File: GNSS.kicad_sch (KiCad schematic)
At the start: 13 parts, among them J8 USB_C_USB2.0_16P, SW5 SW_Push, U6 NEO-M9N

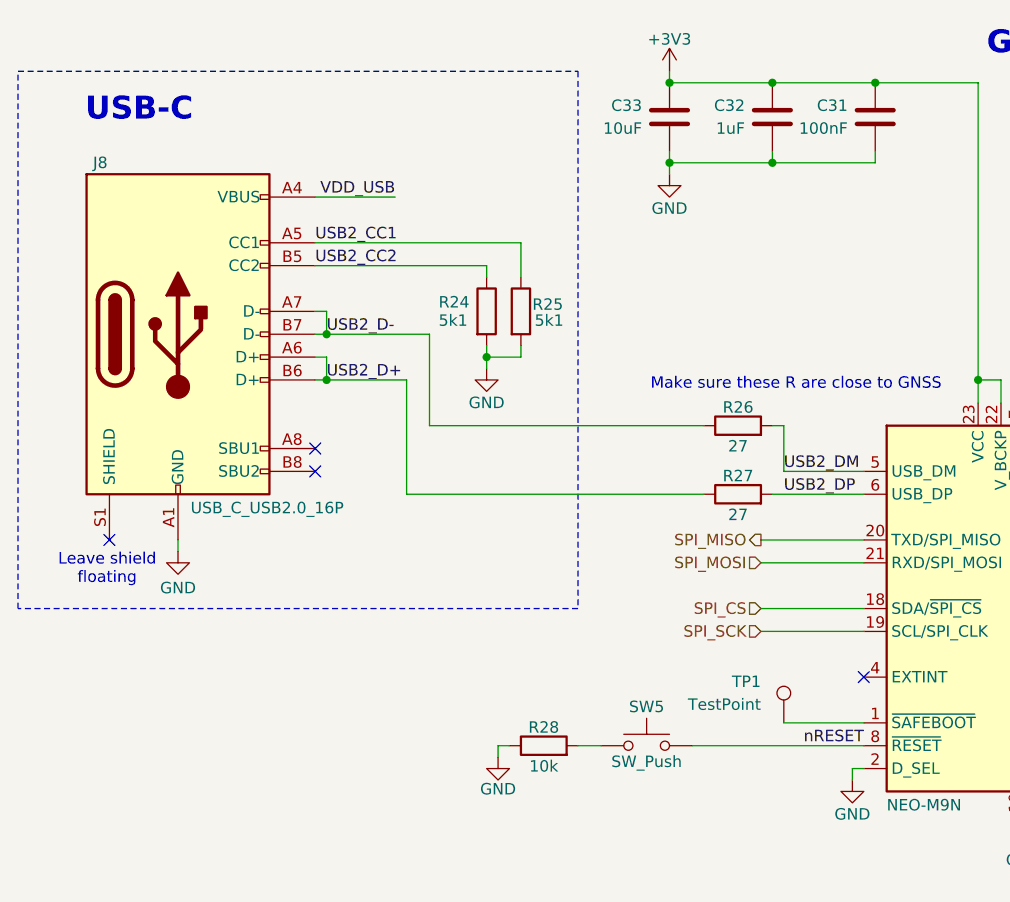
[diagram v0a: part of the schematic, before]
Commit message: Added footprints & routing 30%
- Added Dupont debug headers for UARTs.
- Added footprints: 18650 battery, E32-400M30S.
- Remove Battery Charger due to reliability issue.
- Routing 5V SMPS, 3V3 Regulator, Battery Holder.
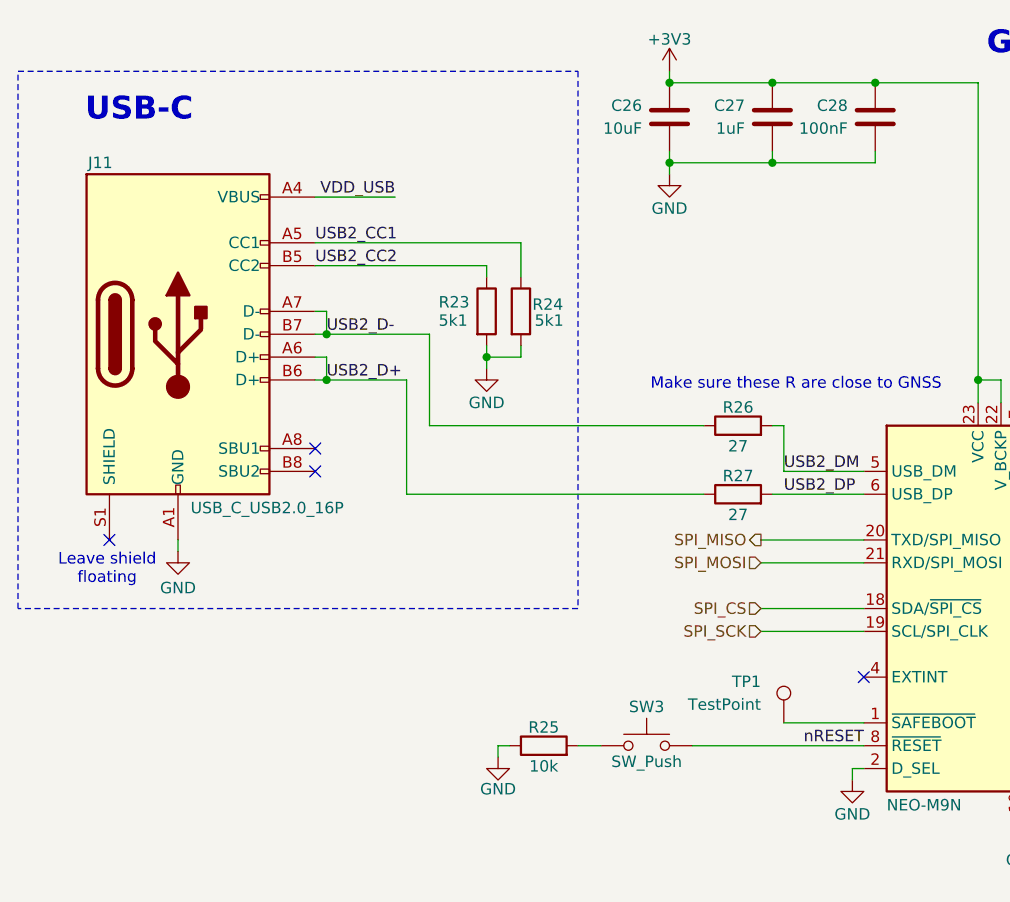
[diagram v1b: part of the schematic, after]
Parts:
- TP1: footprint (none) -> TestPoint:TestPoint_Pad_D2.5mm
- renumbered C33 to C26, C32 to C27, C31 to C28, J8 to J11, R24 to R23, R25 to R24, R28 to R25, SW5 to SW3
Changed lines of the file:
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@@
 		(on_board yes)
 		(dnp no)
-		(property "Reference" "#PWR079"
+		(property "Reference" "#PWR060"
 			(at 118.11 142.24 0)
 			(effects
@@
 			(project "BLV_PCB"
 				(path "/e98ed281-6a46-49b2-ab41-e3d95fdf6973/e5b94b9f-016b-443f-970f-ae0598cc0fac"
-					(reference "#PWR079")
+					(reference "#PWR060")
 					(unit 1)
 				)
@@
 		(on_board yes)
 		(dnp no)
-		(property "Reference" "R28"
+		(property "Reference" "R25"
 			(at 83.82 130.048 90)
 			(effects
@@
 			(project ""
 				(path "/e98ed281-6a46-49b2-ab41-e3d95fdf6973/e5b94b9f-016b-443f-970f-ae0598cc0fac"
-					(reference "R28")
+					(reference "R25")
 					(unit 1)
 				)
@@
 		(on_board yes)
 		(dnp no)
-		(property "Reference" "SW5"
+		(property "Reference" "SW3"
 			(at 95.25 127.762 0)
 			(effects
@@
 			(project "BLV_PCB"
 				(path "/e98ed281-6a46-49b2-ab41-e3d95fdf6973/e5b94b9f-016b-443f-970f-ae0598cc0fac"
-					(reference "SW5")
+					(reference "SW3")
 					(unit 1)
 				)
@@
 		(on_board yes)
 		(dnp no)
-		(property "Reference" "#PWR014"
+		(property "Reference" "#PWR056"
 			(at 77.47 96.52 0)
 			(effects
@@
 			(project "BLV_PCB"
 				(path "/e98ed281-6a46-49b2-ab41-e3d95fdf6973/e5b94b9f-016b-443f-970f-ae0598cc0fac"
-					(reference "#PWR014")
+					(reference "#PWR056")
 					(unit 1)
 				)
@@
 		(on_board yes)
 		(dnp no)
-		(property "Reference" "R24"
+		(property "Reference" "R23"
 			(at 72.136 82.804 0)
 			(effects
@@
 			(project "BLV_PCB"
 				(path "/e98ed281-6a46-49b2-ab41-e3d95fdf6973/e5b94b9f-016b-443f-970f-ae0598cc0fac"
-					(reference "R24")
+					(reference "R23")
 					(unit 1)
 				)
@@
 		(on_board yes)
 		(dnp no)
-		(property "Reference" "#PWR038"
+		(property "Reference" "#PWR055"
 			(at 43.18 116.84 0)
 			(effects
@@
 			(project "BLV_PCB"
 				(path "/e98ed281-6a46-49b2-ab41-e3d95fdf6973/e5b94b9f-016b-443f-970f-ae0598cc0fac"
-					(reference "#PWR038")
+					(reference "#PWR055")
 					(unit 1)
 				)
@@
 		(on_board yes)
 		(dnp no)
-		(property "Reference" "#PWR078"
+		(property "Reference" "#PWR059"
 			(at 97.79 74.93 0)
 			(effects
@@
 			(project "BLV_PCB"
 				(path "/e98ed281-6a46-49b2-ab41-e3d95fdf6973/e5b94b9f-016b-443f-970f-ae0598cc0fac"
-					(reference "#PWR078")
+					(reference "#PWR059")
 					(unit 1)
 				)
@@
 		(on_board yes)
 		(dnp no)
-		(property "Reference" "C32"
+		(property "Reference" "C27"
 			(at 106.172 60.96 0)
 			(effects
@@
 			(project "BLV_PCB"
 				(path "/e98ed281-6a46-49b2-ab41-e3d95fdf6973/e5b94b9f-016b-443f-970f-ae0598cc0fac"
-					(reference "C32")
+					(reference "C27")
 					(unit 1)
 				)
@@
 		(on_board yes)
 		(dnp no)
-		(property "Reference" "C31"
+		(property "Reference" "C28"
 			(at 117.602 60.96 0)
 			(effects
@@
 			(project "BLV_PCB"
 				(path "/e98ed281-6a46-49b2-ab41-e3d95fdf6973/e5b94b9f-016b-443f-970f-ae0598cc0fac"
-					(reference "C31")
+					(reference "C28")
 					(unit 1)
 				)
@@
 		(on_board yes)
 		(dnp no)
-		(property "Reference" "R25"
+		(property "Reference" "R24"
 			(at 82.55 83.058 0)
 			(effects
@@
 			(project "BLV_PCB"
 				(path "/e98ed281-6a46-49b2-ab41-e3d95fdf6973/e5b94b9f-016b-443f-970f-ae0598cc0fac"
-					(reference "R25")
+					(reference "R24")
 					(unit 1)
 				)
@@
 		(on_board yes)
 		(dnp no)
-		(property "Reference" "#PWR081"
+		(property "Reference" "#PWR061"
 			(at 137.16 147.32 0)
 			(effects
@@
 			(project "BLV_PCB"
 				(path "/e98ed281-6a46-49b2-ab41-e3d95fdf6973/e5b94b9f-016b-443f-970f-ae0598cc0fac"
-					(reference "#PWR081")
+					(reference "#PWR061")
 					(unit 1)
 				)
@@
 		(on_board yes)
 		(dnp no)
-		(property "Reference" "C33"
+		(property "Reference" "C26"
 			(at 94.742 60.96 0)
 			(effects
@@
 			(project "BLV_PCB"
 				(path "/e98ed281-6a46-49b2-ab41-e3d95fdf6973/e5b94b9f-016b-443f-970f-ae0598cc0fac"
-					(reference "C33")
+					(reference "C26")
 					(unit 1)
 				)
@@
 		(on_board yes)
 		(dnp no)
-		(property "Reference" "J8"
+		(property "Reference" "J11"
 			(at 34.544 67.31 0)
 			(effects
@@
 			(project "BLV_PCB"
 				(path "/e98ed281-6a46-49b2-ab41-e3d95fdf6973/e5b94b9f-016b-443f-970f-ae0598cc0fac"
-					(reference "J8")
+					(reference "J11")
 					(unit 1)
 				)
@@
 		(on_board yes)
 		(dnp no)
-		(property "Reference" "#PWR076"
+		(property "Reference" "#PWR058"
 			(at 97.79 60.96 0)
 			(effects
@@
 			(project "BLV_PCB"
 				(path "/e98ed281-6a46-49b2-ab41-e3d95fdf6973/e5b94b9f-016b-443f-970f-ae0598cc0fac"
-					(reference "#PWR076")
+					(reference "#PWR058")
 					(unit 1)
 				)
@@
 			)
 		)
-		(property "Footprint" ""
+		(property "Footprint" "TestPoint:TestPoint_Pad_D2.5mm"
 			(at 115.57 129.54 0)
 			(effects
@@
 		(on_board yes)
 		(dnp no)
-		(property "Reference" "#PWR080"
+		(property "Reference" "#PWR057"
 			(at 78.74 139.7 0)
 			(effects
@@
 			(project "BLV_PCB"
 				(path "/e98ed281-6a46-49b2-ab41-e3d95fdf6973/e5b94b9f-016b-443f-970f-ae0598cc0fac"
-					(reference "#PWR080")
-					(unit 1)
-				)
+					(reference "#PWR057")
+					(unit 1)
+				)

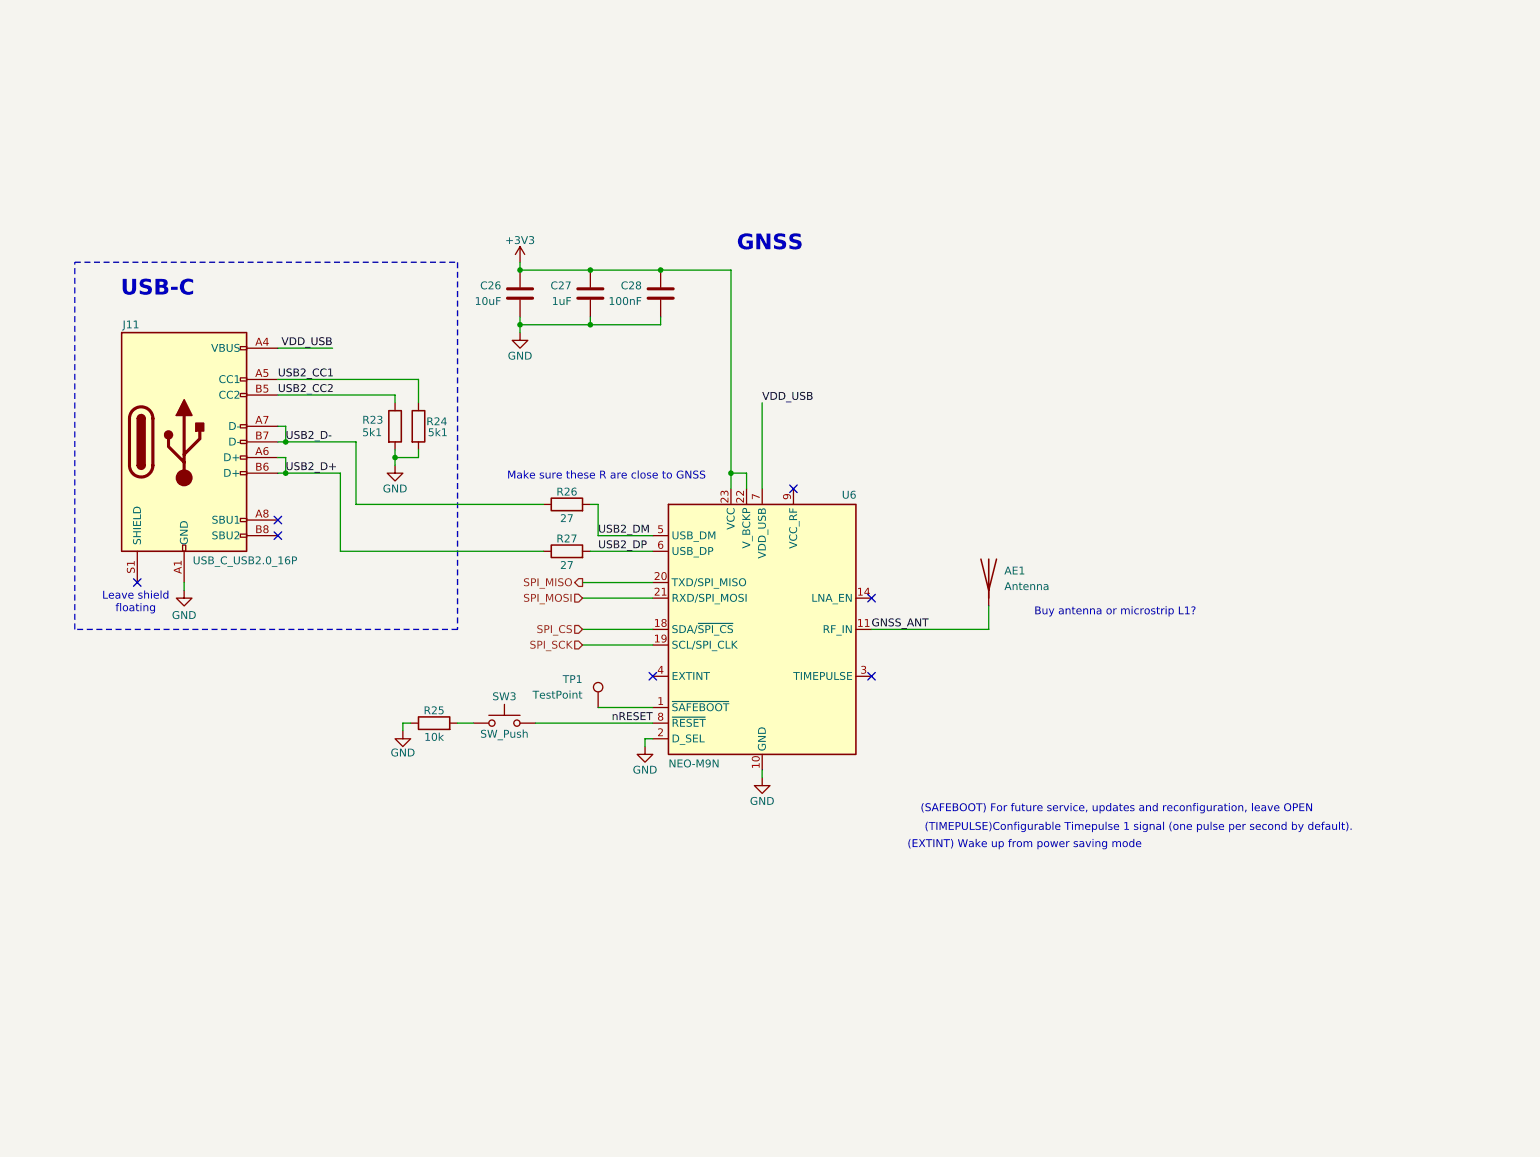
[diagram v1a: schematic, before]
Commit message: Finished layout & DRC
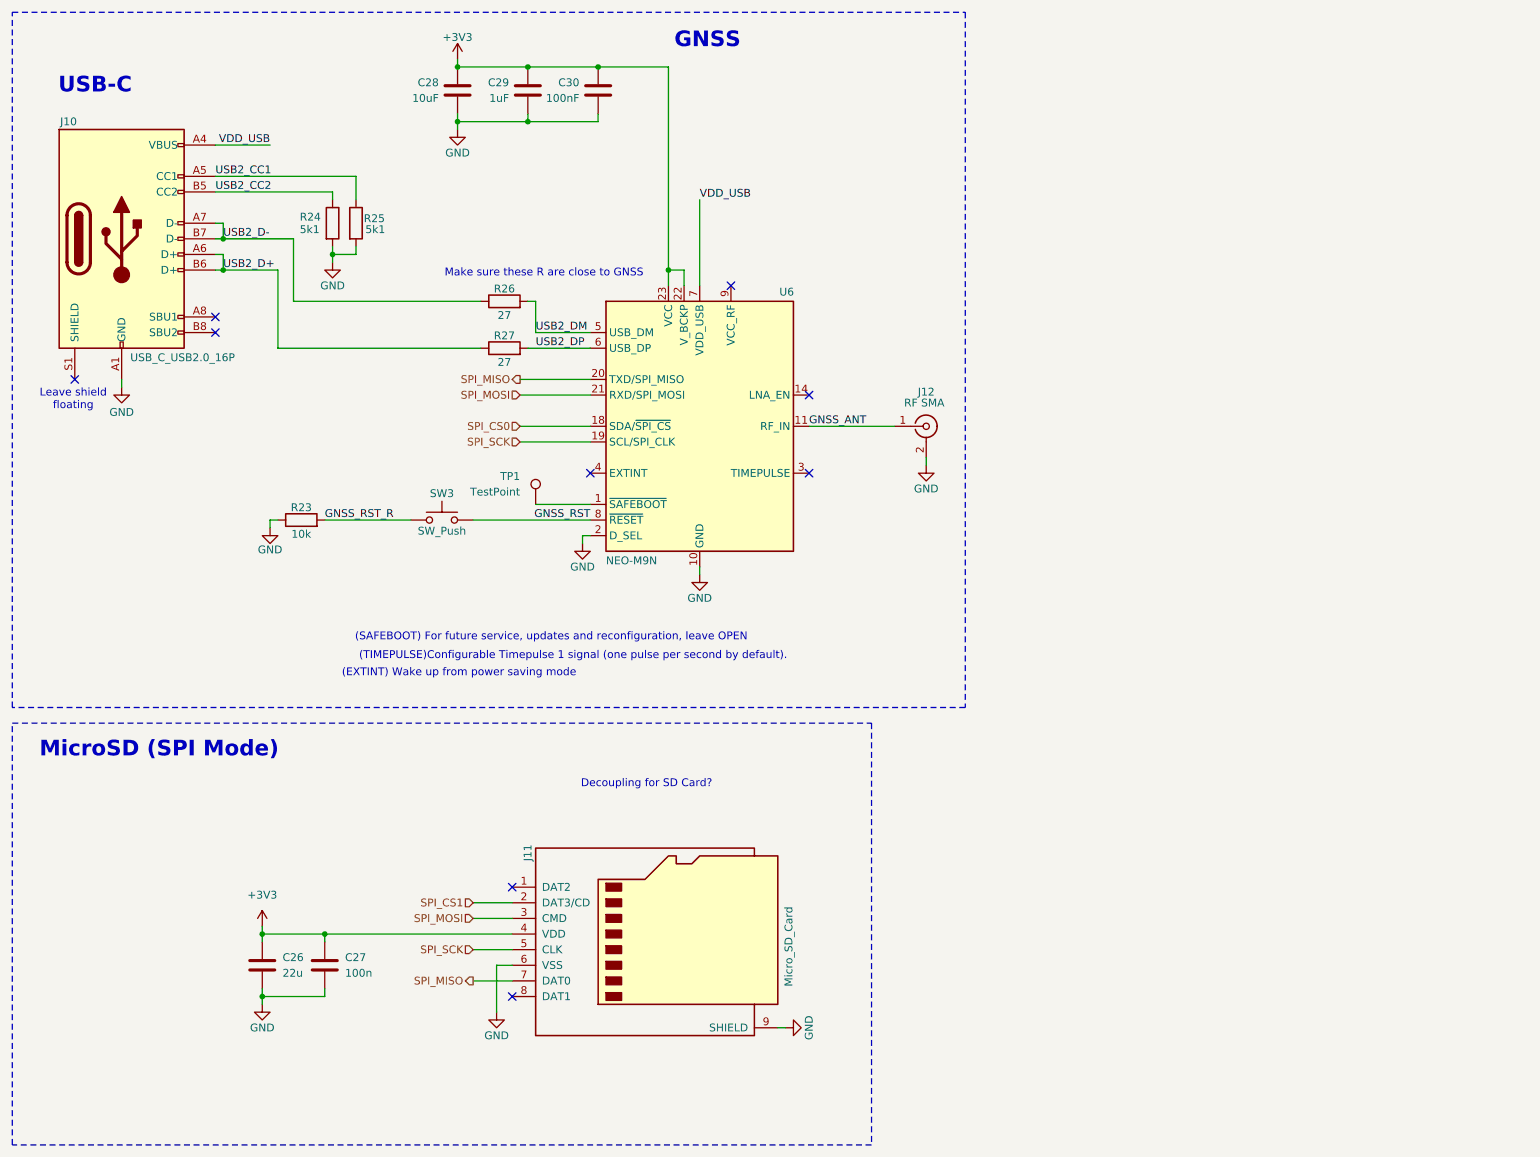
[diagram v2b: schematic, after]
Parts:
- removed AE1: Antenna, symbol Device:Antenna
- added C26: 22u, Capacitor_SMD:C_0805_2012Metric, symbol Device:C
- added C27: 100n, Capacitor_SMD:C_0402_1005Metric, symbol Device:C
- added J11: Micro_SD_Card, Connector_Card:microSD_HC_Wuerth_693072010801, symbol Connector:Micro_SD_Card
- added J12: RF SMA, Connector_Coaxial:SMA_Amphenol_132134_Vertical, symbol Connector:Conn_Coaxial
- J10: renamed from J11; footprint Connector_USB:USB_C_Receptacle_Molex_105450-0101 -> Connector_USB:USB_C_Receptacle_HRO_TYPE-C-31-M-12
- renumbered C26 to C28, C27 to C29, C28 to C30, R25 to R23, R23 to R24, R24 to R25
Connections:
- net +3V3: now also C26.1, C27.1, J11.4 (VDD)
- net GND: now also C26.2, C27.2, J11.6 (VSS), J11.9 (SHIELD), J12.2 (Ext)
- net GNSS_ANT: now also J12.1 (In)
- net SPI_MISO: now also J11.7 (DAT0)
- net SPI_MOSI: now also J11.3 (CMD)
- net SPI_SCK: now also J11.5 (CLK)
- net GNSS_RST_R: now reaches R23.2, SW3.1
- net SPI_CS renamed SPI_CS0
- net nRESET renamed GNSS_RST
- new net SPI_CS1: J11.2 (DAT3/CD)
- no-connect marks 7 -> 9
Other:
- note added: "Decoupling for SD Card?"
- note added: "MicroSD (SPI Mode)"
- note removed: "Buy antenna or microstrip L1?"
- moved on the sheet: C28, C29, C30, J10, R23, R24, R25, R26, R27, SW3, TP1, U6

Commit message: Added silkscreens label description and fixed DRC
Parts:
- TP1: footprint TestPoint:TestPoint_Pad_D2.5mm -> TestPoint:TestPoint_Pad_D1.0mm
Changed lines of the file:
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@@
 			)
 		)
-		(property "Footprint" "TestPoint:TestPoint_Pad_D2.5mm"
+		(property "Footprint" "TestPoint:TestPoint_Pad_D1.0mm"
 			(at 105.41 96.52 0)
 			(effects
